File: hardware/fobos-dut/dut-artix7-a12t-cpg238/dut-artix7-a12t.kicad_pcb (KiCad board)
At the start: 4 copper layers, 92.7 x 76.2 mm, 199 parts, among them J1 Target, J10 Barrel_Jack_Switch, J2 Pmod 2x6, J3 575-8, J4 Glitch, J5 Conn_01x02, J6 Measure, J7 0878321420, J8 575-8, J9 Measure, Q10 BSS138, Q2 BSS138, Q3 BSS138, Q4 BSS138, Q5 BSS138, Q6 BSS138, Q7 FDS9435A, Q8 MMBT3904, Q9 MMBT3904, SW1 SW_DIP_x03, SW2 SW_DIP_x03, U1 TS3A5018DBQR, U10 BGA2801, U11 IS25LP256D-JMLE, U2 SP3003-04ATG, U3 SP3003-04ATG, U4 SP3003-04ATG, U5 SP3003-04ATG, U6 SP3003-04ATG, U7 XC7A12T-CPG238, U8 LTC3569EFE#PBF, U9 INA225

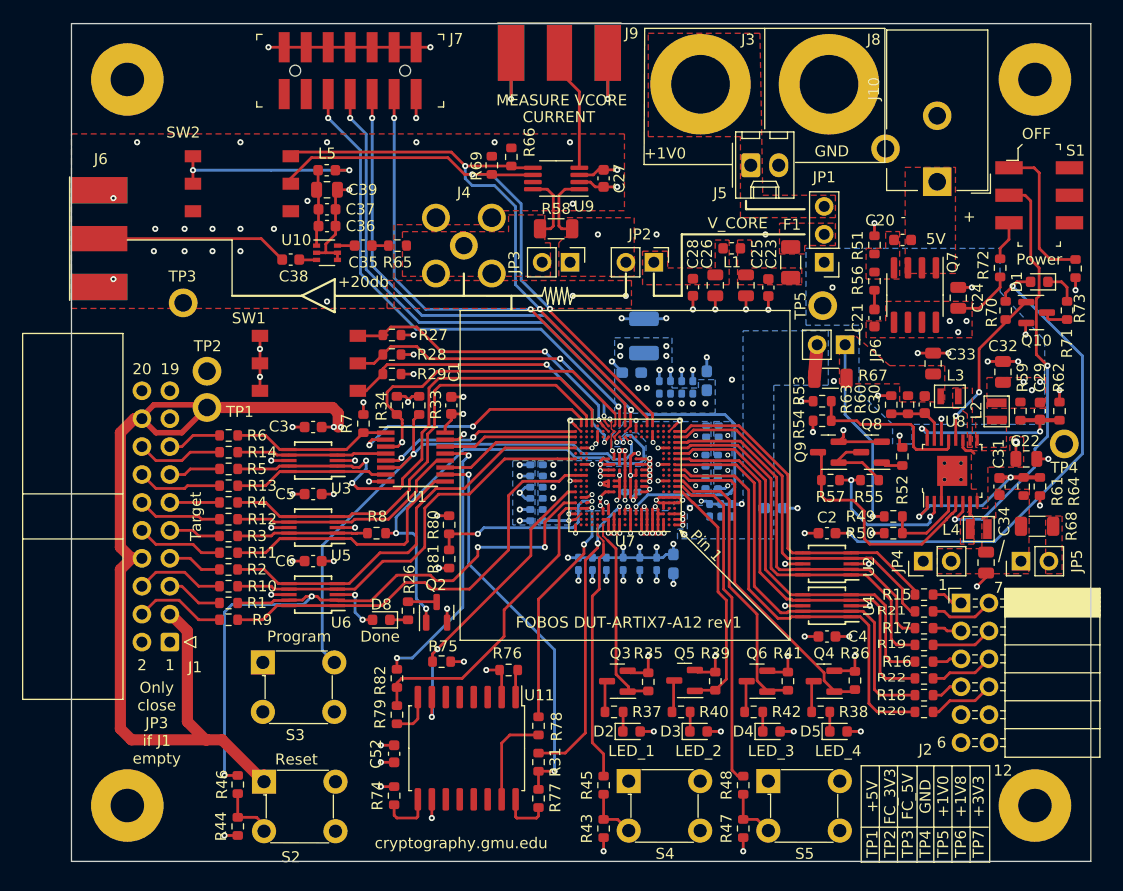
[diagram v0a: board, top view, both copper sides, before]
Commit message: cleaned up FBDA7 rev1 added BOM, fixed bugs in schematic
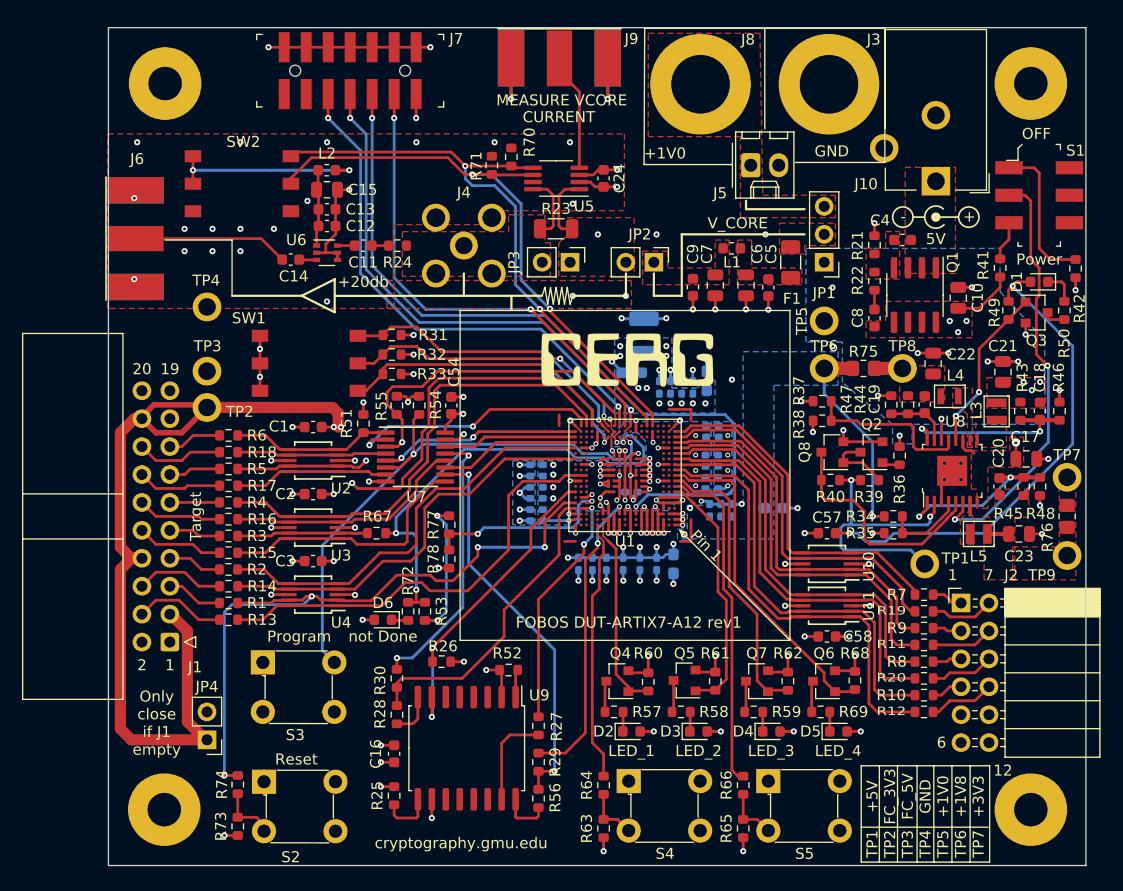
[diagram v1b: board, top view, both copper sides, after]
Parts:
- removed D8: LG_L29K-G2J1-24-Z, LED_SMD:LED_0603_1608Metric
- removed JP5: Shunt3V3, Connector_PinHeader_2.54mm:PinHeader_1x02_P2.54mm_Vertical
- removed JP6: Shunt1V8, Connector_PinHeader_2.54mm:PinHeader_1x02_P2.54mm_Vertical
- removed the Q2 at (132.8, 124.4)
- removed the R26 at (130.2, 124.2)
- removed the U7 at (150.0, 111.9)
- added D6: LG_L29K-G2J1-24-Z, LED_SMD:LED_0603_1608Metric, F.Cu at (128.0, 125.0)
- added G***: LOGO, cerg:cerg_logo, F.Cu at (150.2, 101.4)
- added R53: 200R, Resistor_SMD:R_0603_1608Metric, F.Cu at (131.8, 124.3)
- added R72: 200R, Resistor_SMD:R_0603_1608Metric, F.Cu at (130.3, 124.3)
- added REF**: Symbol_Barrel_Polarity, Symbol:Symbol_Barrel_Polarity, F.Cu at (178.2, 88.3)
- added TP6: 5281, cerg:5281, F.Cu at (168.1, 102.2)
- added TP7: 5281, cerg:5281, F.Cu at (190.2, 112.1)
- added TP8: 5281, cerg:5281, F.Cu at (175.2, 102.2)
- added TP9: 5281, cerg:5281, F.Cu at (190.2, 119.2)
- added U1: XC7A12T-CPG238, Package_BGA:Xilinx_CPG238, F.Cu at (150.0, 111.9)
- JP3: value Shunt1V -> Shunt1R
- R75: renamed from R67; value 0R1 -> 0.1R; footprint Resistor_SMD:R_1206_3216Metric -> Resistor_SMD:R_0805_2012Metric_Pad1.20x1.40mm_HandSolder
- R76: renamed from R68; value 0R1 -> 0.1R; footprint Resistor_SMD:R_1206_3216Metric -> Resistor_SMD:R_0805_2012Metric_Pad1.20x1.40mm_HandSolder
- moved JP4 67.1 mm to (112.0, 136.0), turned to 180 degrees
- moved TP1 16.7 mm to (177.2, 119.9)
- moved C23 3.97 mm to (185.8, 117.2), turned to 0 degrees
- moved H2 3.46 mm to (108.2, 76.3)
- moved H1 3.38 mm to (108.1, 142.3)
- moved J6 3.30 mm to (105.5, 90.4)
- moved R75 3.14 mm to (171.7, 102.2)
- moved R76 2.88 mm to (190.2, 115.6), turned to 90 degrees
- moved TP4 2.20 mm to (112.0, 96.6)
- moved TP5 1.40 mm to (168.1, 97.9)
- moved H3 0.53 mm to (186.9, 142.3)
- moved H4 0.53 mm to (186.9, 76.3)
- moved J9 0.50 mm to (144.0, 74.0)
- moved L5 0.44 mm to (181.4, 117.2)
- moved Q8 0.37 mm to (168.8, 109.8)
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- renumbered C3 to C1, C24 to C10, C35 to C11, C36 to C12, C37 to C13, C38 to C14, C39 to C15, C52 to C16, C22 to C17, C29 to C18, C30 to C19, C5 to C2, C31 to C20, C32 to C21, C33 to C22, C34 to C23, C27 to C24, C40 to C25, C41 to C26, C42 to C27, C43 to C28, C44 to C29, C6 to C3, C45 to C30, C46 to C31, C47 to C32, C48 to C33, C49 to C34, C50 to C35, C51 to C36, C7 to C37, C8 to C38, C10 to C39, C20 to C4, C11 to C40, C12 to C41, C19 to C42, C15 to C43, C16 to C44, C17 to C45, C18 to C46, C14 to C47, C53 to C48, C54 to C49, C23 to C5, C55 to C50, C56 to C51, C57 to C52, C58 to C53, C1 to C54, C9 to C55, C13 to C56, C2 to C57, C4 to C58, C25 to C6, C26 to C7, C21 to C8, C28 to C9, J8 to J3, J3 to J8, L5 to L2, L2 to L3, L3 to L4, L4 to L5, Q7 to Q1, Q8 to Q2, Q10 to Q3, Q3 to Q4, Q4 to Q6, Q6 to Q7, Q9 to Q8, R18 to R10, R19 to R11, R20 to R12, R9 to R13, R10 to R14, R11 to R15, R12 to R16, R13 to R17, R14 to R18, R21 to R19, R22 to R20, R51 to R21, R56 to R22, R58 to R23, R65 to R24, R74 to R25, R75 to R26, R78 to R27, R79 to R28, R31 to R29, R82 to R30, R27 to R31, R28 to R32, R29 to R33, R49 to R34, R50 to R35, R52 to R36, R53 to R37, R54 to R38, R55 to R39, R57 to R40, R72 to R41, R73 to R42, R59 to R43, R60 to R44, R61 to R45, R62 to R46, R63 to R47, R64 to R48, R70 to R49, R71 to R50, R7 to R51, R76 to R52, R33 to R54, R34 to R55, R77 to R56, R37 to R57, R40 to R58, R42 to R59, R35 to R60, R39 to R61, R41 to R62, R43 to R63, R45 to R64, R47 to R65, R48 to R66, R8 to R67, R36 to R68, R38 to R69, R15 to R7, R66 to R70, R69 to R71, R44 to R73, R46 to R74, R80 to R77, R81 to R78, R16 to R8, R17 to R9, TP4 to TP1, TP1 to TP2, TP2 to TP3, TP3 to TP4, U2 to U10, U4 to U11, U3 to U2, U5 to U3, U6 to U4, U9 to U5, U10 to U6, U1 to U7, U11 to U9
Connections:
- C19 pad 1: pre1V8 -> /Power/pre1V8
- C20 pad 1: pre3V3 -> /Power/pre3V3
- C22 pad 1: pre1V8 -> /Power/pre1V8
- C23 pad 1: pre3V3 -> /Power/pre3V3
- C24 pad 1: +5V -> FC_3V3
- JP4 pad 2: pre3V3 -> +3V3
- L4 pad 2: pre1V8 -> /Power/pre1V8
- L5 pad 2: pre3V3 -> /Power/pre3V3
- R34 pad 2: pre1V8 -> +1V8
- R44 pad 2: pre1V8 -> /Power/pre1V8
- R45 pad 2: pre3V3 -> /Power/pre3V3
- R75 pad 1: pre1V8 -> /Power/pre1V8
- R76 pad 1: pre3V3 -> /Power/pre3V3
- U5 pad 3: +5V -> FC_3V3
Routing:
- net pre1V8: track 17.7 -> 0.00 mm, vias 1 -> 0
- net +1V8: track 6.29 -> 22.2 mm, vias 4 -> 5
- net +3V3: track 58.8 -> 70.1 mm, vias 35 -> 36
- net +5V: track 30.3 -> 38.8 mm, vias 9 -> 8
- net (no net): track 0.00 -> 8.00 mm
- net Net-(J6-In): track 17.4 -> 14.1 mm
- net FC_3V3: track 199.0 -> 196.3 mm
- net Net-(Q2-D): track 2.62 -> 0.00 mm
- net /Power/pre1V8: track 0.00 -> 2.54 mm
- net /Power/pre3V3: track 0.00 -> 1.92 mm
- net Net-(D8-K): track 1.74 -> 0.00 mm
- net Net-(D6-Pad1): track 0.00 -> 1.52 mm
- net GND: track 220.3 -> 219.0 mm, vias 147 -> 145
- net SW_DONE: track 42.7 -> 42.1 mm
- net Net-(Q2-C): track 6.90 -> 6.29 mm
- added copper zone on F.Cu, net /Power/pre1V8
- added copper zone on F.Cu, net /Power/pre3V3
- removed copper zone on F.Cu, net pre1V8
- removed copper zone on F.Cu, net pre3V3
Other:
- board size 92.7 x 76.2 mm -> 88.9 x 76.2 mm
- board text added: "Only close if J1 empty"
- board text added: "not Done"
- board text removed: "Done"
- board text removed: "Only close JP3 if J1 empty"
- board text removed: "VCCINT"
